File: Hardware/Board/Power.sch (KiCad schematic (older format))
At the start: 97 parts, among them Q100 2N7002, Q101 2N7002, Q102 2N7002, Q103 2N7002, U100 TPS54160DGQR, U101 TPS54160DGQR, U102 TPS54160DGQR, U103 TPS54360DDA, U104 TPS54360DDA

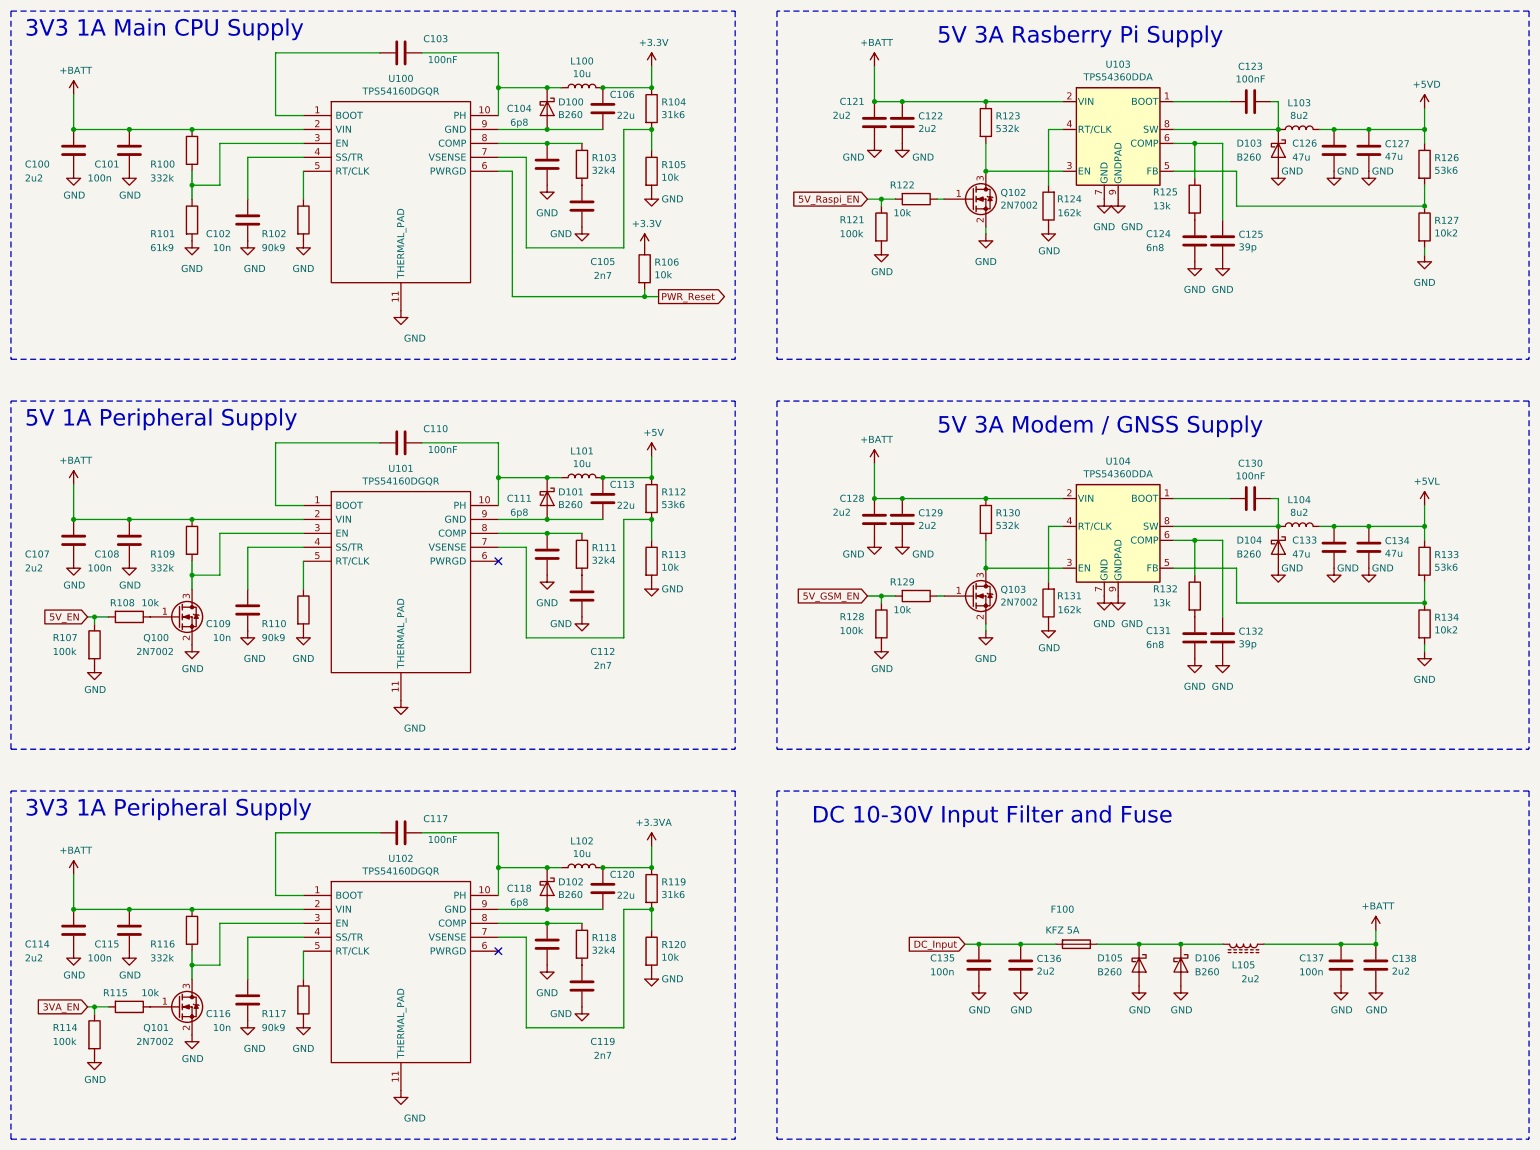
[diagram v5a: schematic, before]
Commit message: Board: Änderung Footprints, Debug geroutet, Beginn Platzierung Netzteil, Bezeichnungen und Werte aufgeräumt.
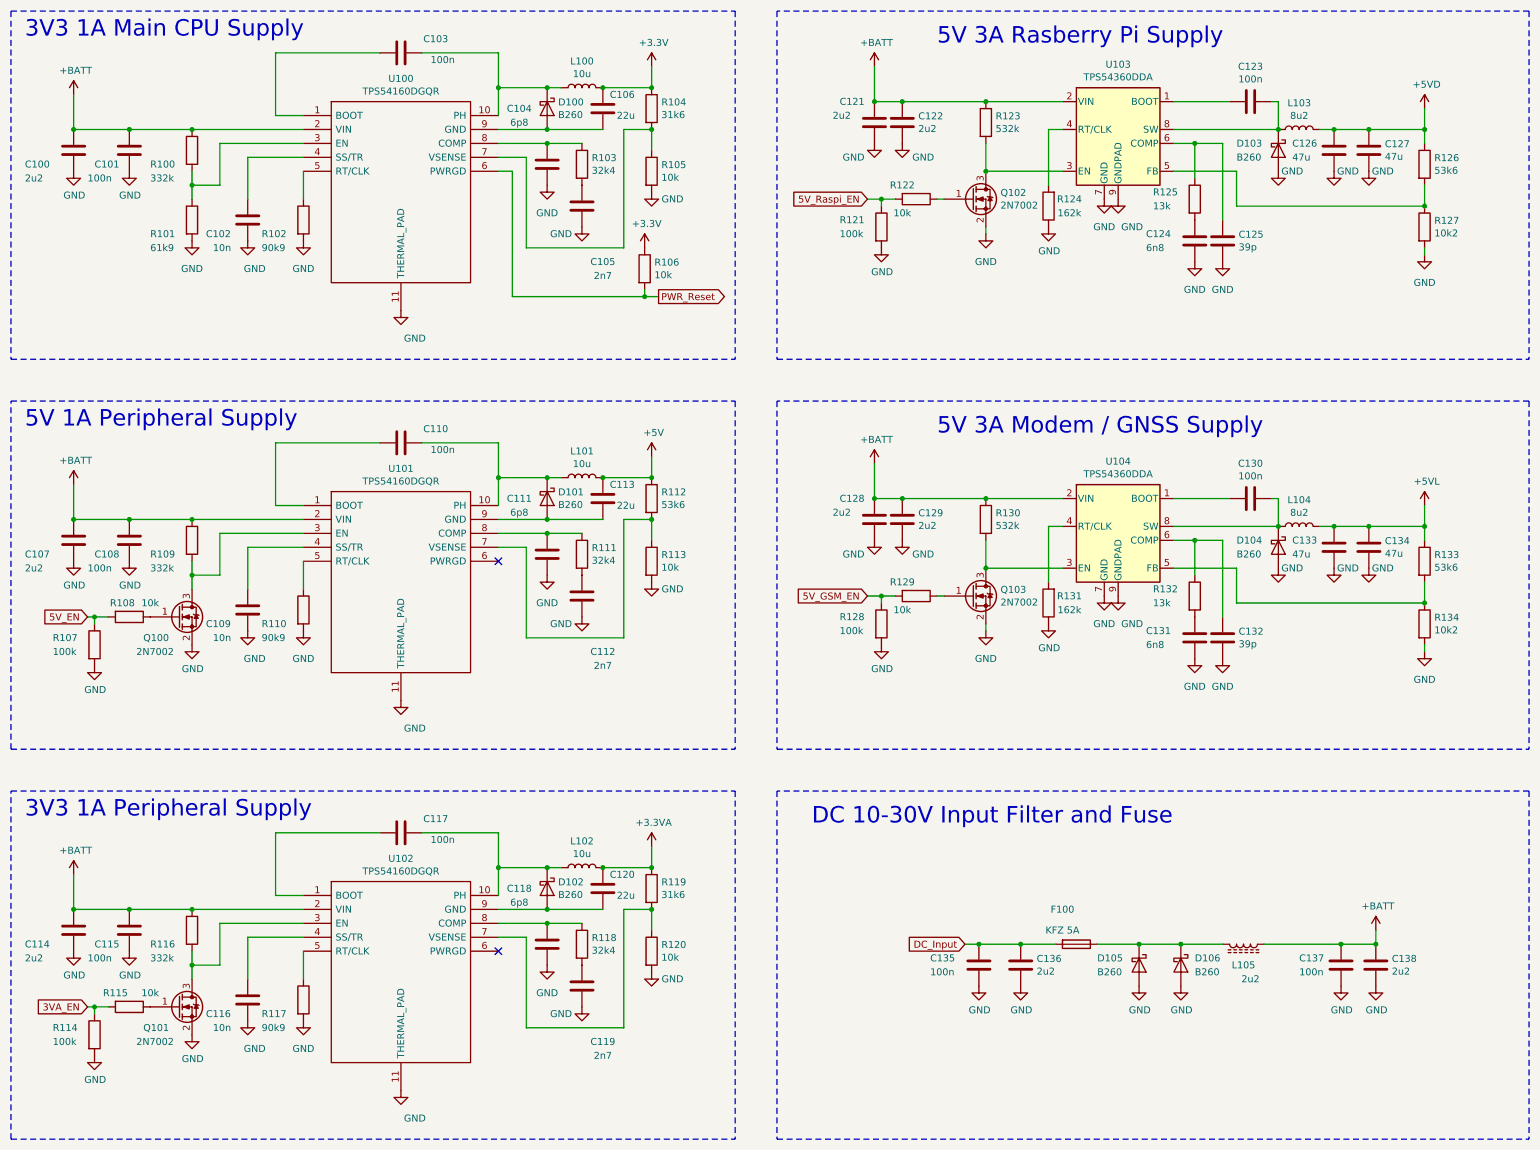
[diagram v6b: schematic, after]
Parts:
- C103, C110, C117, C123, C130: value 100nF -> 100n
- L103, L104: footprint Womo-Lin:XAL8080 -> Inductor_SMD:L_Coilcraft_XAL60xx_6.36x6.56mm
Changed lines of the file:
@@
 F 0 "L103" V 10540 1650 50  0000 C CNN
 F 1 "8u2" V 10449 1650 50  0000 C CNN
-F 2 "Womo-Lin:XAL8080" H 10350 1650 50  0001 C CNN
+F 2 "Inductor_SMD:L_Coilcraft_XAL60xx_6.36x6.56mm" H 10350 1650 50  0001 C CNN
 F 3 "~" H 10350 1650 50  0001 C CNN
 	1    10350 1650
@@
 AR Path="/5E0C5EEA/5CA4FE23" Ref="C?"  Part="1"
 F 0 "C123" V 9748 1450 50  0000 C CNN
-F 1 "100nF" V 9839 1450 50  0000 C CNN
+F 1 "100n" V 9839 1450 50  0000 C CNN
 F 2 "Capacitor_SMD:C_0603_1608Metric" H 10038 1300 50  0001 C CNN
 F 3 "~" H 10000 1450 50  0001 C CNN
@@
 AR Path="/5E0C5EEA/5CA770E9" Ref="C?"  Part="1"
 F 0 "C103" V 3800 1350 50  0000 C CNN
-F 1 "100nF" V 3950 1400 50  0000 C CNN
+F 1 "100n" V 3950 1400 50  0000 C CNN
 F 2 "Capacitor_SMD:C_0603_1608Metric" H 3938 950 50  0001 C CNN
 F 3 "~" H 3900 1100 50  0001 C CNN
@@
 F 0 "L104" V 10540 4500 50  0000 C CNN
 F 1 "8u2" V 10449 4500 50  0000 C CNN
-F 2 "Womo-Lin:XAL8080" H 10350 4500 50  0001 C CNN
+F 2 "Inductor_SMD:L_Coilcraft_XAL60xx_6.36x6.56mm" H 10350 4500 50  0001 C CNN
 F 3 "~" H 10350 4500 50  0001 C CNN
 	1    10350 4500
@@
 AR Path="/5E0C5EEA/5ECE3145" Ref="C?"  Part="1"
 F 0 "C130" V 9748 4300 50  0000 C CNN
-F 1 "100nF" V 9839 4300 50  0000 C CNN
+F 1 "100n" V 9839 4300 50  0000 C CNN
 F 2 "Capacitor_SMD:C_0603_1608Metric" H 10038 4150 50  0001 C CNN
 F 3 "~" H 10000 4300 50  0001 C CNN
@@
 AR Path="/5E0C5EEA/5ECBB35F" Ref="C?"  Part="1"
 F 0 "C110" V 3800 4150 50  0000 C CNN
-F 1 "100nF" V 3950 4200 50  0000 C CNN
+F 1 "100n" V 3950 4200 50  0000 C CNN
 F 2 "Capacitor_SMD:C_0603_1608Metric" H 3938 3750 50  0001 C CNN
 F 3 "~" H 3900 3900 50  0001 C CNN
@@
 AR Path="/5E0C5EEA/5ED5E9D8" Ref="C?"  Part="1"
 F 0 "C117" V 3800 6950 50  0000 C CNN
-F 1 "100nF" V 3950 7000 50  0000 C CNN
+F 1 "100n" V 3950 7000 50  0000 C CNN
 F 2 "Capacitor_SMD:C_0603_1608Metric" H 3938 6550 50  0001 C CNN
 F 3 "~" H 3900 6700 50  0001 C CNN

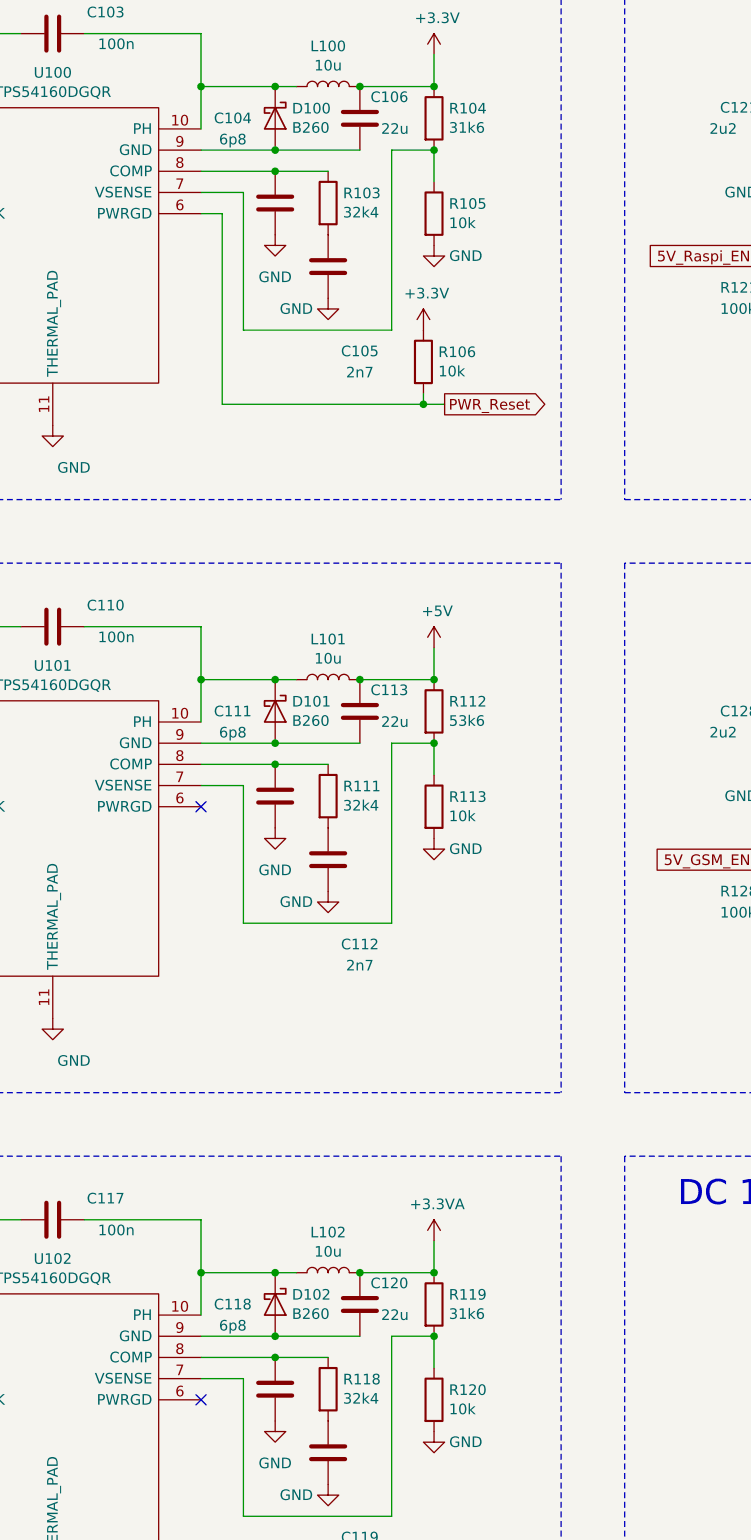
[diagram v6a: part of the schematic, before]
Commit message: Board: PSU platziert, Fehlerkorrektur, Routing PSU
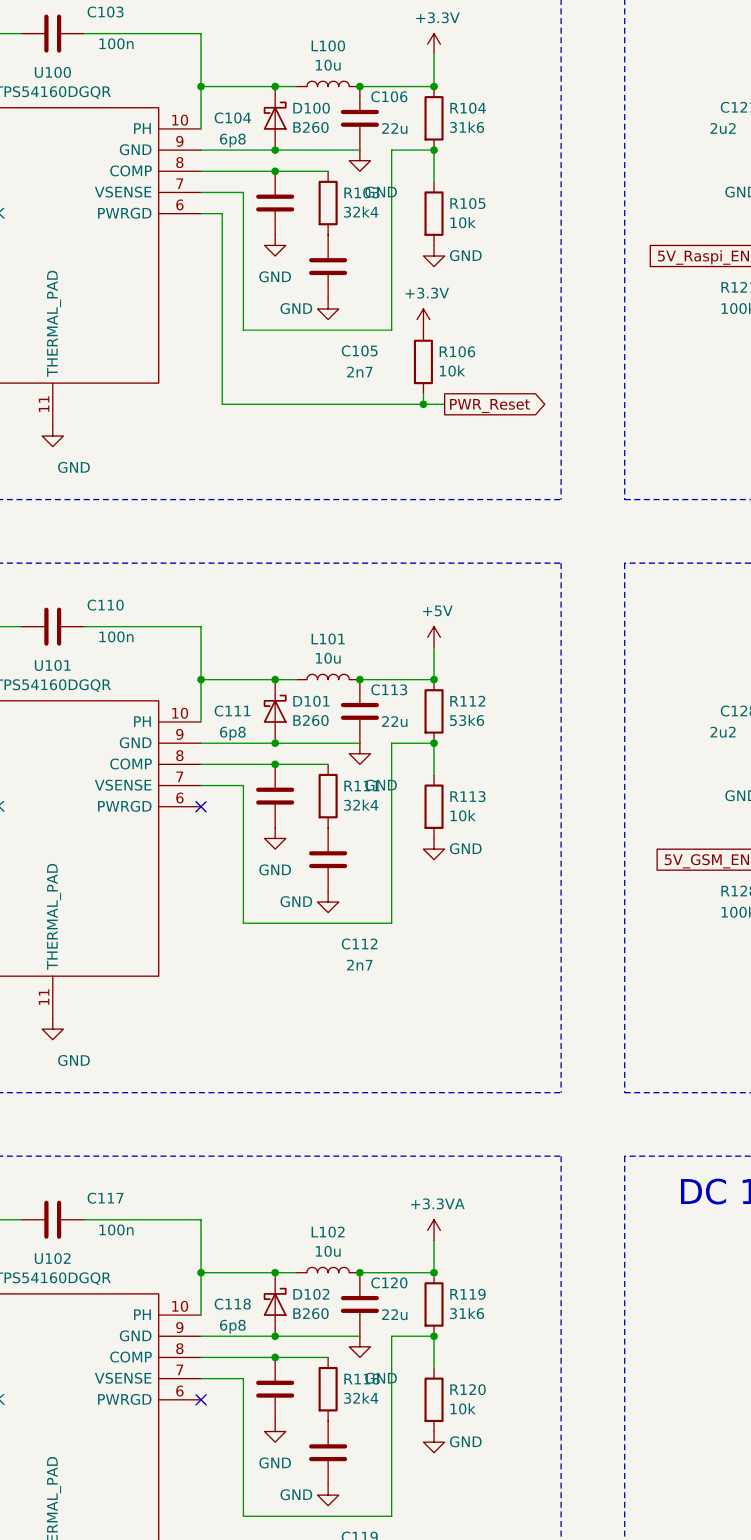
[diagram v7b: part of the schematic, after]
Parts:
- D103, D104, D105, D106: footprint Diode_SMD:D_SMB -> Diode_SMD:D_SMC
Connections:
- net GND: now also C106.2, C113.2, C120.2, D100.2 (A), D101.2 (A), D102.2 (A), U100.9 (GND), U101.9 (GND), U102.9 (GND)
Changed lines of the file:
@@
 F 0 "D103" V 10150 1500 50  0000 L CNN
 F 1 "B260" V 10250 1500 50  0000 L CNN
-F 2 "Diode_SMD:D_SMB" H 10200 1625 50  0001 C CNN
+F 2 "Diode_SMD:D_SMC" H 10200 1625 50  0001 C CNN
 F 3 "http://www.jameco.com/Jameco/Products/ProdDS/1538777.pdf" H 10200 1800 50  0001 C CNN
 	1    10200 1800
@@
 F 0 "D104" V 10150 4350 50  0000 L CNN
 F 1 "B260" V 10250 4350 50  0000 L CNN
-F 2 "Diode_SMD:D_SMB" H 10200 4475 50  0001 C CNN
+F 2 "Diode_SMD:D_SMC" H 10200 4475 50  0001 C CNN
 F 3 "http://www.jameco.com/Jameco/Products/ProdDS/1538777.pdf" H 10200 4650 50  0001 C CNN
 	1    10200 4650
@@
 F 0 "D105" V 9150 7350 50  0000 L CNN
 F 1 "B260" V 9250 7350 50  0000 L CNN
-F 2 "Diode_SMD:D_SMB" H 9200 7475 50  0001 C CNN
+F 2 "Diode_SMD:D_SMC" H 9200 7475 50  0001 C CNN
 F 3 "http://www.jameco.com/Jameco/Products/ProdDS/1538777.pdf" H 9200 7650 50  0001 C CNN
 	1    9200 7650
@@
 F 0 "D106" V 9450 7750 50  0000 L CNN
 F 1 "B260" V 9550 7750 50  0000 L CNN
-F 2 "Diode_SMD:D_SMB" H 9500 7475 50  0001 C CNN
+F 2 "Diode_SMD:D_SMC" H 9500 7475 50  0001 C CNN
 F 3 "http://www.jameco.com/Jameco/Products/ProdDS/1538777.pdf" H 9500 7650 50  0001 C CNN
 	1    9500 7650
@@
 	1    0    0    -1
 $EndComp
+$Comp
+L Womo-rescue:GND-power #PWR?
+U 1 1 65D1D777
+P 5350 1650
+AR Path="/5C8BBC9A/65D1D777" Ref="#PWR?"  Part="1"
+AR Path="/5E0C5EEA/65D1D777" Ref="#PWR?"  Part="1"
+F 0 "#PWR?" H 5350 1400 50  0001 C CNN
+F 1 "GND" H 5450 1450 50  0000 C CNN
+F 2 "" H 5350 1650 50  0001 C CNN
+F 3 "" H 5350 1650 50  0001 C CNN
+	1    5350 1650
+	1    0    0    -1
+$EndComp
+$Comp
+L Womo-rescue:GND-power #PWR?
+U 1 1 65D286B4
+P 5350 4450
+AR Path="/5C8BBC9A/65D286B4" Ref="#PWR?"  Part="1"
+AR Path="/5E0C5EEA/65D286B4" Ref="#PWR?"  Part="1"
+F 0 "#PWR?" H 5350 4200 50  0001 C CNN
+F 1 "GND" H 5450 4250 50  0000 C CNN
+F 2 "" H 5350 4450 50  0001 C CNN
+F 3 "" H 5350 4450 50  0001 C CNN
+	1    5350 4450
+	1    0    0    -1
+$EndComp
+$Comp
+L Womo-rescue:GND-power #PWR?
+U 1 1 65D337CD
+P 5350 7250
+AR Path="/5C8BBC9A/65D337CD" Ref="#PWR?"  Part="1"
+AR Path="/5E0C5EEA/65D337CD" Ref="#PWR?"  Part="1"
+F 0 "#PWR?" H 5350 7000 50  0001 C CNN
+F 1 "GND" H 5450 7050 50  0000 C CNN
+F 2 "" H 5350 7250 50  0001 C CNN
+F 3 "" H 5350 7250 50  0001 C CNN
+	1    5350 7250
+	1    0    0    -1
+$EndComp
